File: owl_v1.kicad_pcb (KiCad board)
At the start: 2 copper layers, 59 parts, among them J1 USB_C_Receptacle_USB2.0_16P, J10 JST-PH Battery, J2 SWD, J3 Screw_Terminal_01x03, J4 SPI1_IMU, J5 I2C, J6 Micro_SD_Card_Det_Hirose_DM3AT, J7 I2C OLED, J8 External GPIOs, U1 STM32F103C8T6, U3 FT230XS, U4 SN65HVD230, U5 TLV73333PDBV, Y1 8MHz, Y2 32k768

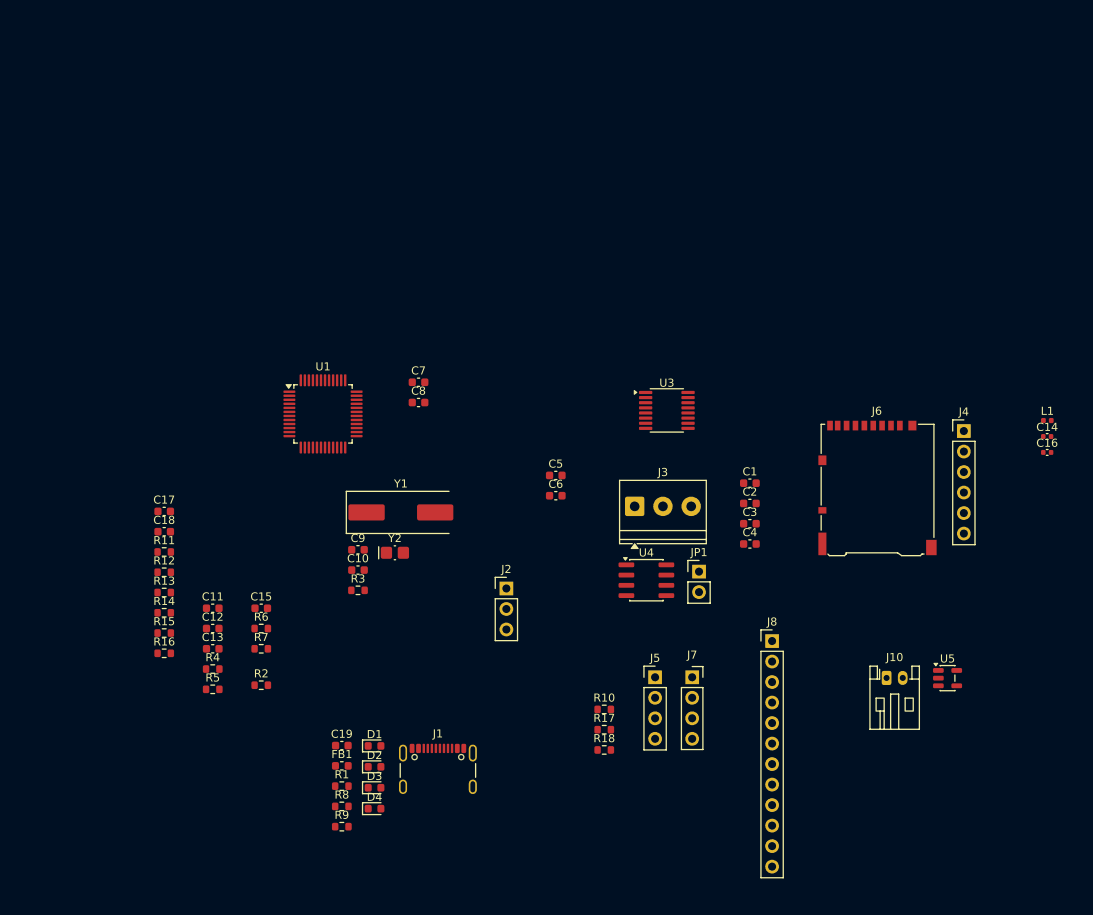
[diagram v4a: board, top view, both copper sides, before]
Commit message: [feat] Initial routing for the owl PCB
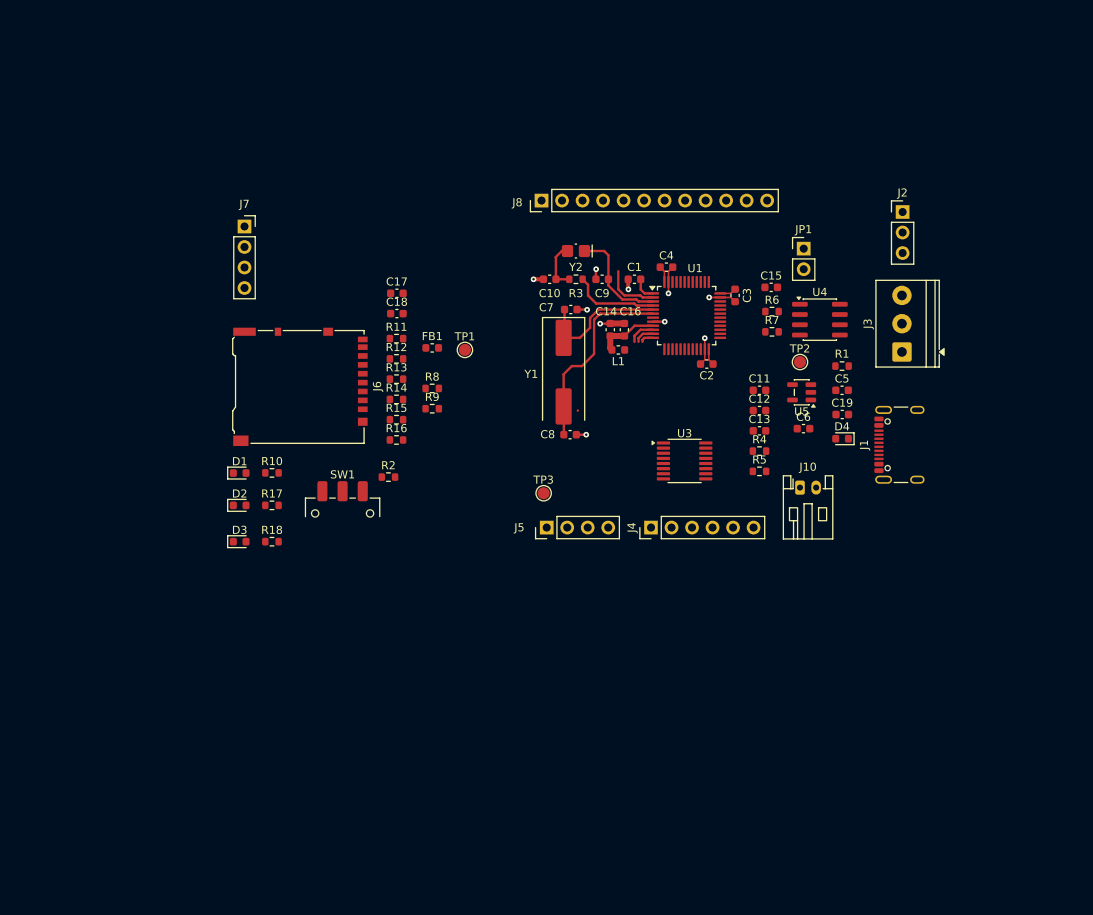
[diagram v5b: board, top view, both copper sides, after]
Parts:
- added SW1: SW_SPDT, Button_Switch_SMD:SW_SPDT_CK_JS102011SAQN, F.Cu at (132.1, 106.0)
- added TP1: ~, TestPoint:TestPoint_Pad_D1.5mm, F.Cu at (147.2, 85.8)
- added TP2: ~, TestPoint:TestPoint_Pad_D1.5mm, F.Cu at (188.8, 87.2)
- added TP3: ~, TestPoint:TestPoint_Pad_D1.5mm, F.Cu at (157.0, 103.5)
- C14, C16: footprint Capacitor_SMD:C_0402_1005Metric -> Capacitor_SMD:C_0603_1608Metric
- L1: footprint Inductor_SMD:L_0402_1005Metric -> Inductor_SMD:L_0603_1608Metric
- moved R1 80.9 mm to (194.0, 87.8), turned to 180 degrees
- moved J7 78.7 mm to (120.0, 70.5)
- moved C15 74.6 mm to (185.2, 78.0)
- moved R6 74.4 mm to (185.3, 81.0)
- moved R7 74.4 mm to (185.3, 83.5)
- moved C19 74.3 mm to (194.0, 93.8)
- moved D4 73.8 mm to (194.0, 96.8), turned to 180 degrees
- moved C11 72.9 mm to (183.7, 90.8)
- moved C13 72.9 mm to (183.7, 95.8)
- moved R4 72.9 mm to (183.7, 98.3)
- moved C12 72.9 mm to (183.7, 93.3)
- moved R5 72.9 mm to (183.7, 100.8)
- moved J6 72.6 mm to (126.9, 90.3), turned to -90 degrees
- moved J1 71.4 mm to (202.2, 97.5), turned to 90 degrees
- moved J2 67.7 mm to (201.5, 68.7)
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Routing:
- net HSE_OSC_OUT: track 0.00 -> 24.5 mm
- net GND: track 0.00 -> 20.8 mm, vias 0 -> 10
- net HSE_OSC_IN: track 0.00 -> 16.8 mm
- net LSE_OSC_IN: track 0.00 -> 13.3 mm
- net LSE_OSC_OUT: track 0.00 -> 10.8 mm
- net +3.3V: track 0.00 -> 9.16 mm
- net +3.3VA: track 0.00 -> 7.64 mm
- net GPIO_8: track 0.00 -> 6.96 mm
- net Net-(C10-Pad1): track 0.00 -> 6.17 mm
- net GPIO_0: track 0.00 -> 3.36 mm
- net GPIO_1: track 0.00 -> 2.48 mm
- net GPIO_2: track 0.00 -> 1.65 mm

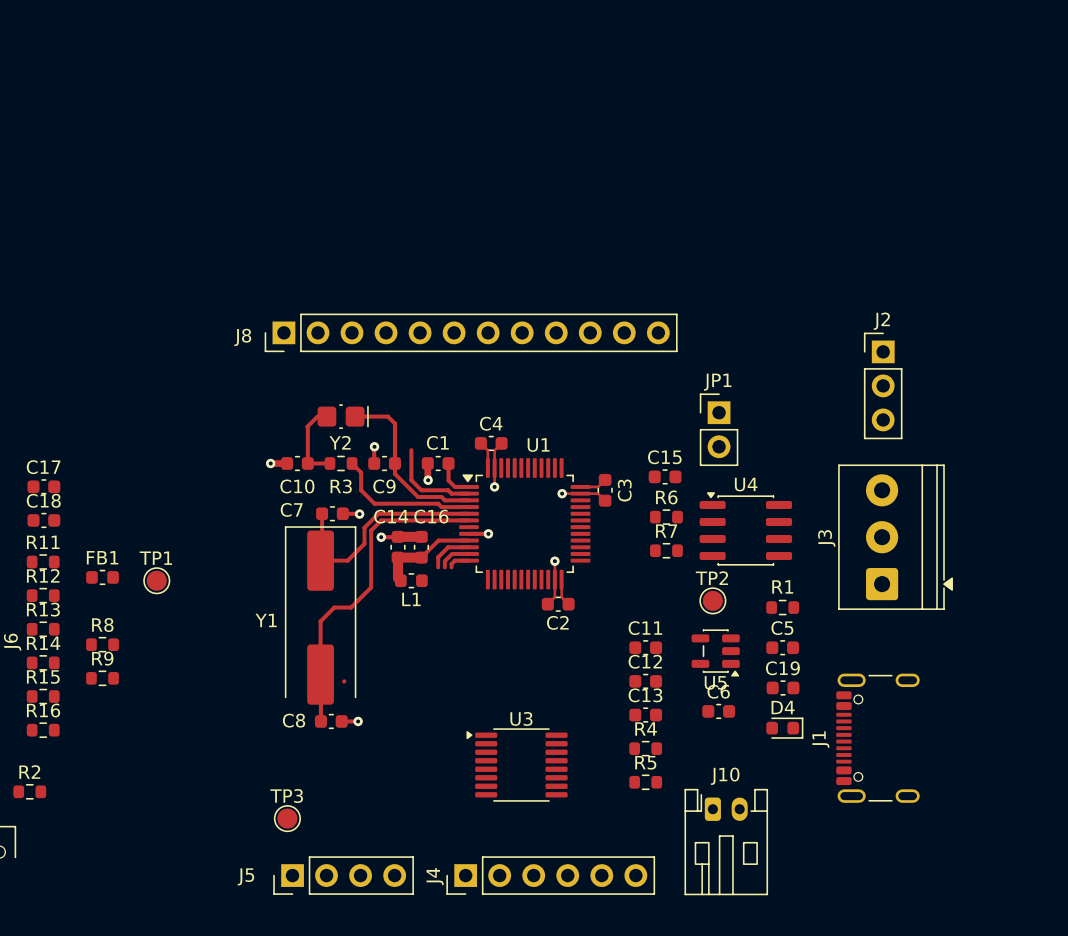
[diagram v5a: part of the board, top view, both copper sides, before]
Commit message: [feat] Finished routing power regulation
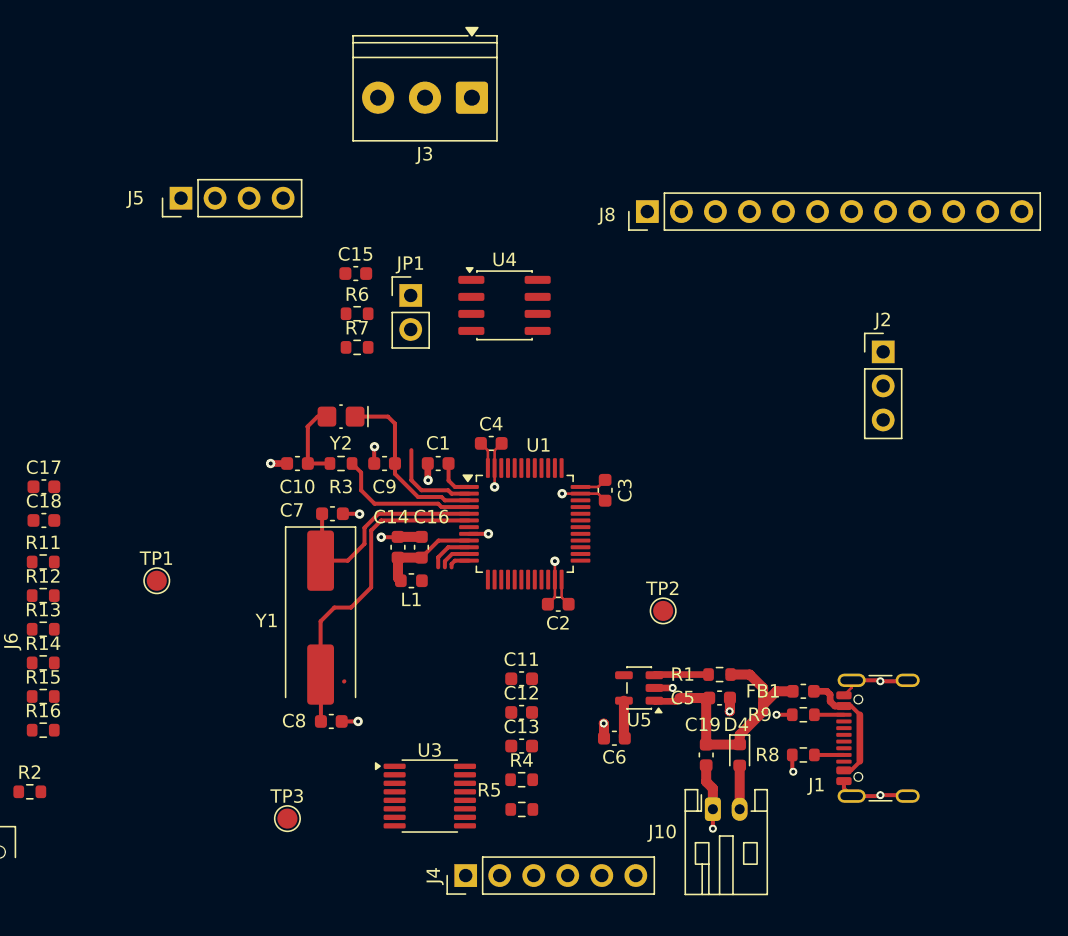
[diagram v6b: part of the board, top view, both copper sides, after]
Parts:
- moved FB1 53.0 mm to (195.5, 94.0)
- moved R8 52.9 mm to (195.5, 98.8), turned to 180 degrees
- moved R9 52.4 mm to (195.5, 95.8), turned to 180 degrees
- moved J5 51.2 mm to (149.1, 57.2)
- moved J3 47.5 mm to (170.8, 49.7), turned to 180 degrees
- moved J8 28.6 mm to (183.9, 58.2)
- moved R7 27.6 mm to (162.2, 68.3)
- moved C15 27.6 mm to (162.1, 62.8)
- moved R6 27.6 mm to (162.2, 65.8)
- moved U4 24.6 mm to (173.2, 65.2)
- moved JP1 24.6 mm to (166.2, 64.5)
- moved C13 9.54 mm to (174.5, 98.1)
- moved C11 9.54 mm to (174.5, 93.1)
- moved C12 9.54 mm to (174.5, 95.6)
- moved R4 9.54 mm to (174.5, 100.6)
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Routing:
- net GND: track 20.8 -> 43.6 mm, vias 10 -> 18
- net VBUS: track 0.00 -> 20.6 mm
- net +5V: track 0.00 -> 9.44 mm
- net Net-(U5-EN): track 0.00 -> 4.06 mm
- net VBAT: track 0.00 -> 3.26 mm
- net +3.3V: track 9.16 -> 12.0 mm
- net Net-(J1-CC2): track 0.00 -> 2.21 mm
- net Net-(J1-CC1): track 0.00 -> 2.21 mm
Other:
- board text added: "D4"

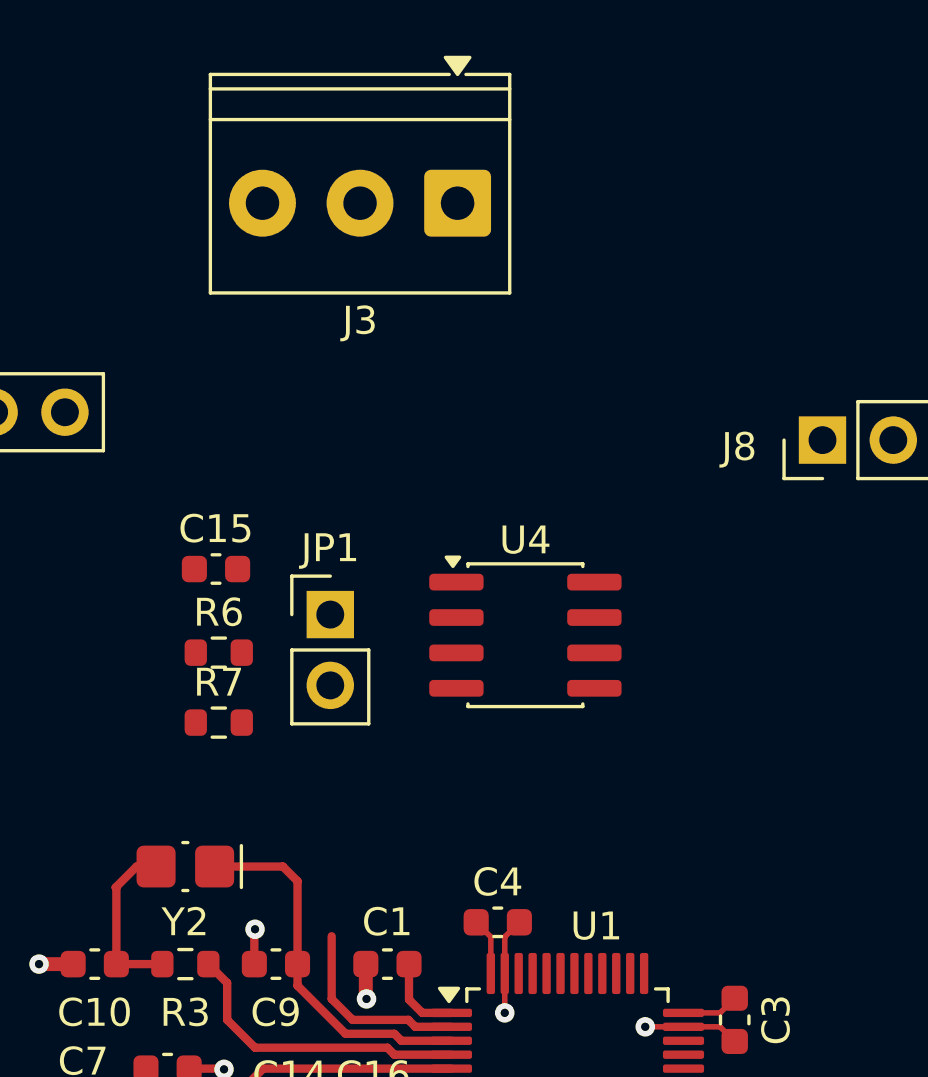
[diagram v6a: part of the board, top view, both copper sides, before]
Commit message: [refactor] Change pinouts for CAN screw terminal
I need to change this because I am struggling to route this in the pcb
editor
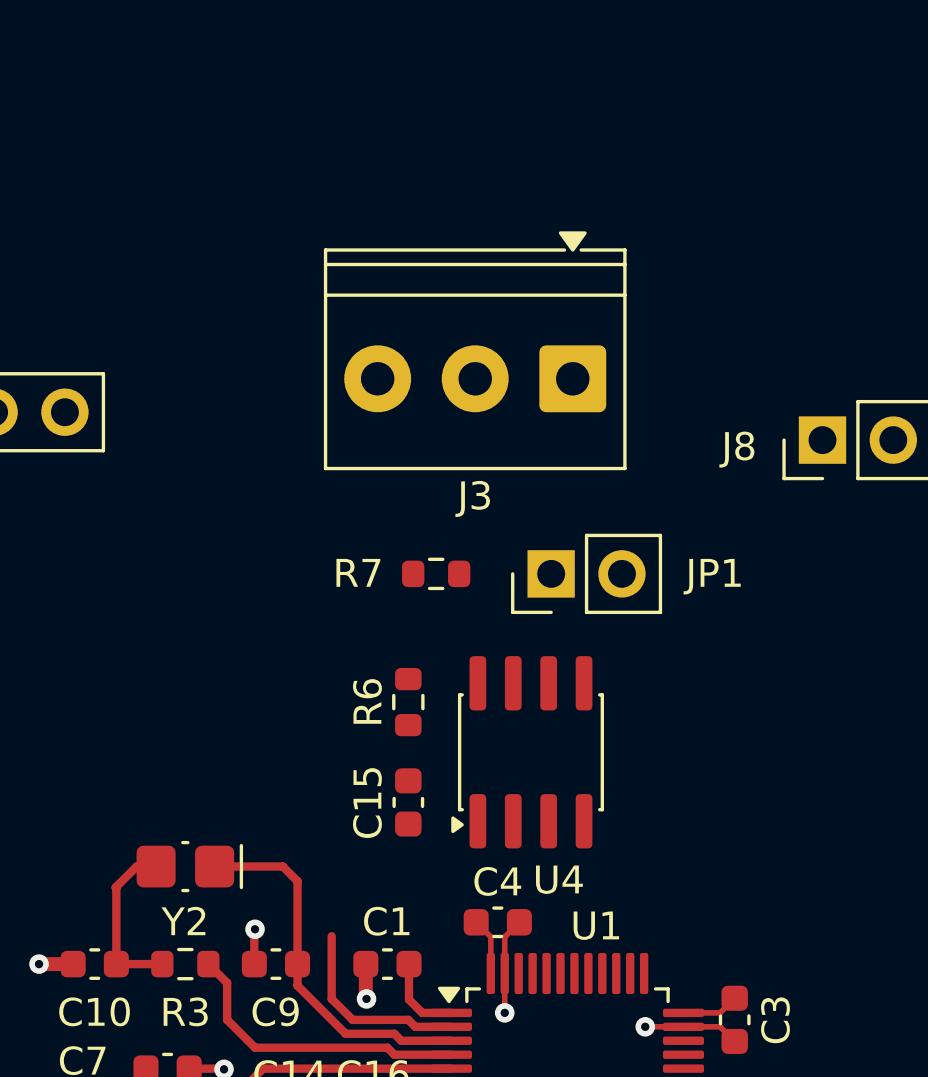
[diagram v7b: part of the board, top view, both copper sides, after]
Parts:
- moved C15 10.9 mm to (169.0, 71.2), turned to 90 degrees
- moved R7 9.45 mm to (170.0, 63.0)
- moved JP1 8.06 mm to (174.1, 63.0), turned to 90 degrees
- moved J3 7.53 mm to (174.9, 56.0)
- moved R6 7.03 mm to (169.0, 67.6), turned to 90 degrees
- moved U4 4.20 mm to (173.4, 69.4), turned to 90 degrees
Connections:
- J3 pad 1: /owl_v1/CAN Transceiver/CAN_H -> GND
- J3 pad 3: GND -> /owl_v1/CAN Transceiver/CAN_H

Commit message: [checkpoint] Checkpoint before I mess up my routing for the micro SD card
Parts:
- moved J6 72.0 mm to (191.2, 58.0), turned to 180 degrees
- moved R5 65.2 mm to (118.6, 136.4)
- moved C11 65.2 mm to (118.5, 126.7)
- moved C12 65.2 mm to (118.5, 129.2)
- moved C13 65.2 mm to (118.5, 131.7)
- moved R4 65.2 mm to (118.5, 134.2)
- moved J4 62.8 mm to (118.3, 143.0), turned to -90 degrees
- moved TP3 50.0 mm to (109.2, 118.0)
- moved J1 41.9 mm to (168.6, 122.6), turned to 0 degrees
- moved C17 40.4 mm to (176.8, 92.3)
- moved C18 40.4 mm to (176.8, 94.9)
- moved R11 40.4 mm to (176.8, 98.0)
- moved R12 40.4 mm to (176.8, 100.5)
- moved R13 40.4 mm to (176.8, 103.0)
- moved R14 40.4 mm to (176.8, 105.5)
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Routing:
- net +3.3V: track 12.0 -> 28.6 mm
- net GND: track 43.6 -> 59.3 mm, vias 18 -> 20
- net /owl_v1/CAN Transceiver/CAN_L: track 0.00 -> 14.6 mm
- net /owl_v1/CAN Transceiver/CAN_H: track 0.00 -> 14.3 mm
- net CAN_RX: track 0.00 -> 7.13 mm
- net CAN_TX: track 0.00 -> 6.97 mm
- net Net-(U1-BOOT0): track 0.00 -> 5.96 mm
- net I2C_SDA: track 0.00 -> 5.62 mm
- net I2C_SCLK: track 0.00 -> 5.35 mm
- net LED_GREEN: track 0.00 -> 5.22 mm
- net LED_BLUE: track 0.00 -> 4.94 mm
- net TRACE_SWO: track 0.00 -> 4.39 mm
- net GPIO_7: track 0.00 -> 4.38 mm
- net SWCLK: track 0.00 -> 3.97 mm
- net VBUS: track 20.6 -> 24.0 mm
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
